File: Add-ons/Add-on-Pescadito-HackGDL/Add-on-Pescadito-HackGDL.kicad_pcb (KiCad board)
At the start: 2 copper layers, 153.2 x 94.5 mm, 96 parts, among them J1 Conn_02x03_Odd_Even, J2 Conn_02x03_Odd_Even, J3 Conn_02x03_Odd_Even, J4 Conn_02x03_Odd_Even, J5 Conn_02x03_Odd_Even, J6 Conn_02x03_Odd_Even, SW1 SW_RST, SW10 On, SW11 SW_RST, SW12 On, SW2 On, SW3 SW_RST, SW4 On, SW5 SW_RST, SW6 On, SW7 SW_RST, SW8 On, SW9 SW_RST, U1 PY32F002AA15M6TU, U2 PY32F002AA15M6TU, U3 PY32F002AA15M6TU, U4 PY32F002AA15M6TU, U5 PY32F002AA15M6TU, U6 PY32F002AA15M6TU

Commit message: feat(Hw):Update_Route_And_Init_Addon_Tortuguita
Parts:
- BT1, BT2, BT3, BT4, BT5, C1, C2, C3, C4, C5, J1, J2, J3, J4, J5, R1, R10, R11, R12, R13, R14, R15, R16, R17, R18, R19, R2, R20, R21, R22, R23, R24, R25, R3, R4, R5, R6, R7, R8, R9, SW1, SW10, SW2, SW3, SW4, SW5, SW6, SW7, SW8, SW9, U1, U2, U3, U4, U5: moved to B.Cu
- moved R15 295.1 mm to (222.6, 85.5), turned to 180 degrees
- moved R11 285.6 mm to (213.3, 67.9)
- moved R10 278.3 mm to (171.0, 85.5), turned to 180 degrees
- moved SW6 277.5 mm to (222.4, 64.7), turned to -41 degrees
- moved BT3 270.7 mm to (206.6, 84.9), turned to -15 degrees
- moved R6 269.4 mm to (161.7, 67.9)
- moved R13 264.2 mm to (191.4, 82.6), turned to -90 degrees
- moved SW5 264.2 mm to (208.5, 61.2), turned to 180 degrees
- moved D11 263.2 mm to (215.9, 66.1), turned to 139 degrees
- moved R12 262.7 mm to (190.6, 66.7)
- moved SW4 262.3 mm to (170.8, 64.7), turned to -41 degrees
- moved R14 253.8 mm to (181.7, 71.7), turned to -90 degrees
- moved J3 252.0 mm to (187.8, 85.2)
- moved BT2 250.9 mm to (155.0, 84.9), turned to -15 degrees
- moved D15 250.5 mm to (202.2, 85.1), turned to 155 degrees
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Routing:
- net /Pink_Fish/+3.3V: track 0.00 -> 77.2 mm, vias 0 -> 4
- net /Green_Fish/+3.3V: track 0.00 -> 76.1 mm, vias 0 -> 4
- net /Blue_Fish/+3.3V: track 0.00 -> 75.9 mm, vias 0 -> 4
- net /Red_Fish/+3.3V: track 0.00 -> 75.4 mm, vias 0 -> 4
- net /Orange_Fish/+3.3V: track 0.00 -> 74.6 mm, vias 0 -> 4
- net /Yellow_Fish/+3.3V: track 0.00 -> 74.2 mm, vias 0 -> 4
- net Net-(BT5--): track 0.00 -> 29.5 mm, vias 0 -> 2
- net Net-(BT4--): track 0.00 -> 29.3 mm, vias 0 -> 2
- net Net-(BT1--): track 0.00 -> 29.3 mm, vias 0 -> 2
- net Net-(BT3--): track 0.00 -> 29.1 mm, vias 0 -> 2
- net Net-(BT2--): track 0.00 -> 29.0 mm, vias 0 -> 2
- net Net-(BT6--): track 0.00 -> 28.8 mm, vias 0 -> 2
- net /Orange_Fish/PA6: track 0.00 -> 23.4 mm, vias 0 -> 1
- net /Pink_Fish/PA6: track 0.00 -> 23.4 mm, vias 0 -> 1
- net /Yellow_Fish/PA6: track 0.00 -> 23.4 mm, vias 0 -> 1
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- added copper zone on B.Cu, net /Blue_Fish/GND
- added copper zone on F.Cu, net /Blue_Fish/GND
- added copper zone on B.Cu, net /Green_Fish/GND
- added copper zone on F.Cu, net /Green_Fish/GND
- added copper zone on B.Cu, net /Orange_Fish/GND
- added copper zone on F.Cu, net /Orange_Fish/GND
- added copper zone on B.Cu, net /Pink_Fish/GND
- added copper zone on F.Cu, net /Pink_Fish/GND
- added copper zone on B.Cu, net /Red_Fish/GND
- added copper zone on F.Cu, net /Red_Fish/GND
- added copper zone on B.Cu, net /Yellow_Fish/GND
- added copper zone on F.Cu, net /Yellow_Fish/GND
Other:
- outline, holes or cut-outs redrawn

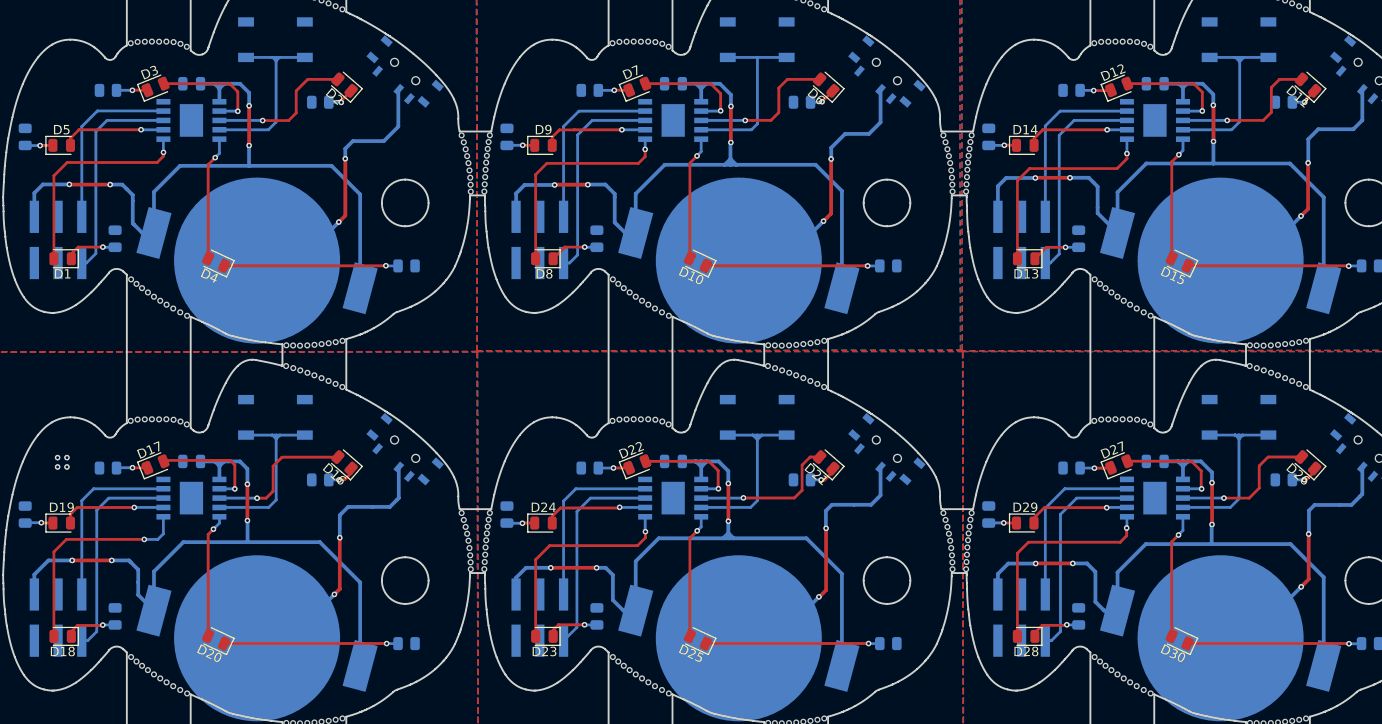
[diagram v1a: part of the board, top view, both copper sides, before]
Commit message: feat(Hw):Update_Labels
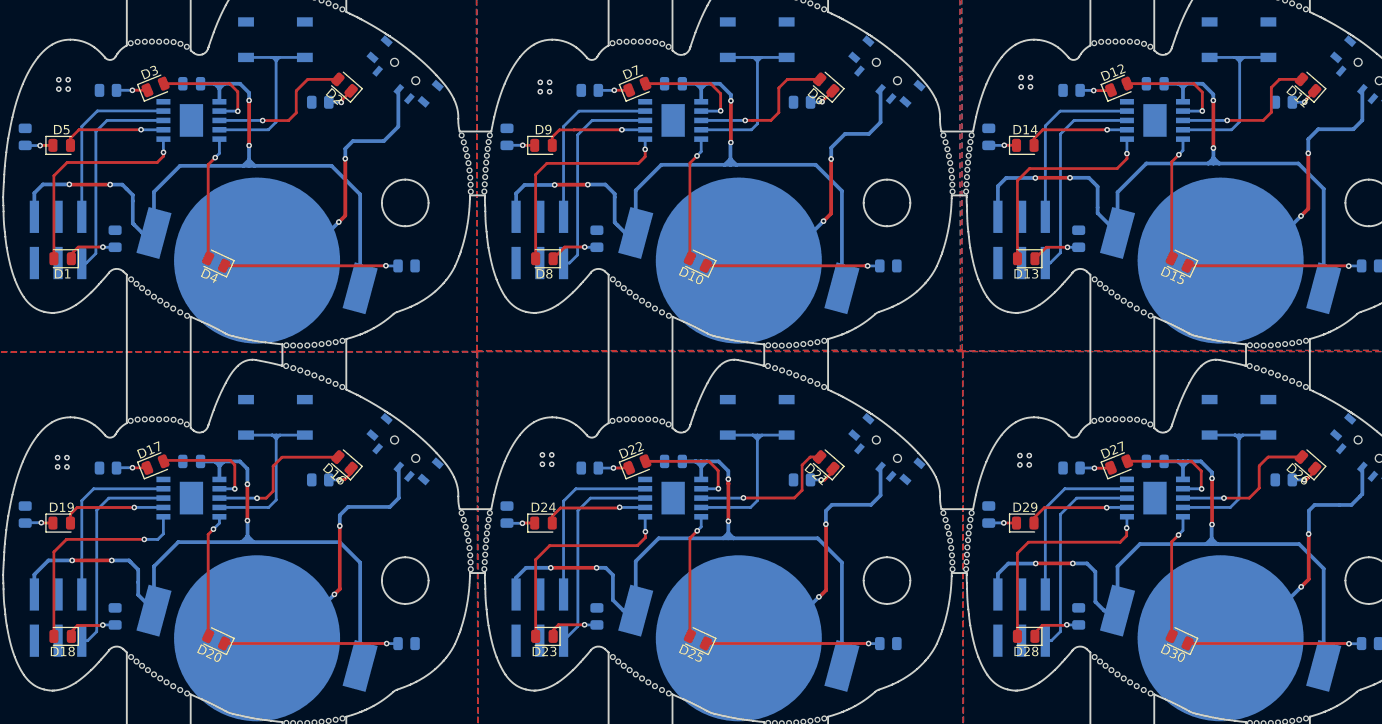
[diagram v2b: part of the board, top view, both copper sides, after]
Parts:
- added kibuzzard-684B03BD: G***, kibuzzard-684B03BD, B.Cu at (164.5, 64.3)
- added kibuzzard-684B03BD: G***, kibuzzard-684B03BD, B.Cu at (216.1, 104.7)
- added kibuzzard-684B03BD: G***, kibuzzard-684B03BD, B.Cu at (164.5, 104.7)
- added kibuzzard-684B03BD: G***, kibuzzard-684B03BD, B.Cu at (112.9, 64.3)
- added kibuzzard-684B03BD: G***, kibuzzard-684B03BD, B.Cu at (216.1, 64.3)
- added kibuzzard-684B03BD: G***, kibuzzard-684B03BD, B.Cu at (112.9, 104.7)
- added kibuzzard-684B03C9: G***, kibuzzard-684B03C9, B.Cu at (167.9, 108.6)
- added kibuzzard-684B03C9: G***, kibuzzard-684B03C9, B.Cu at (219.5, 108.6)
- added kibuzzard-684B03C9: G***, kibuzzard-684B03C9, B.Cu at (219.5, 68.2)
- added kibuzzard-684B03C9: G***, kibuzzard-684B03C9, B.Cu at (116.3, 68.2)
- added kibuzzard-684B03C9: G***, kibuzzard-684B03C9, B.Cu at (167.9, 68.2)
- added kibuzzard-684B03C9: G***, kibuzzard-684B03C9, B.Cu at (116.3, 108.6)
- added kibuzzard-68929515: G***, kibuzzard-68929515, B.Cu at (84.2, 77.5)
- added kibuzzard-68929515: G***, kibuzzard-68929515, B.Cu at (84.2, 117.9)
- added kibuzzard-68929515: G***, kibuzzard-68929515, B.Cu at (187.4, 77.5)
- added kibuzzard-68929515: G***, kibuzzard-68929515, B.Cu at (187.4, 117.9)
- added kibuzzard-68929515: G***, kibuzzard-68929515, B.Cu at (135.8, 77.5)
- added kibuzzard-68929515: G***, kibuzzard-68929515, B.Cu at (135.8, 117.9)
- added kibuzzard-68929520: G***, kibuzzard-68929520, B.Cu at (79.5, 117.9)
- added kibuzzard-68929520: G***, kibuzzard-68929520, B.Cu at (182.6, 77.5)
- added kibuzzard-68929520: G***, kibuzzard-68929520, B.Cu at (131.1, 117.9)
- added kibuzzard-68929520: G***, kibuzzard-68929520, B.Cu at (79.5, 77.5)
- added kibuzzard-68929520: G***, kibuzzard-68929520, B.Cu at (182.6, 117.9)
- added kibuzzard-68929520: G***, kibuzzard-68929520, B.Cu at (131.1, 77.5)
- added kibuzzard-6892952E: G***, kibuzzard-6892952E, B.Cu at (140.3, 125.3)
- added kibuzzard-6892952E: G***, kibuzzard-6892952E, B.Cu at (140.3, 84.8)
- added kibuzzard-6892952E: G***, kibuzzard-6892952E, B.Cu at (88.7, 125.3)
- added kibuzzard-6892952E: G***, kibuzzard-6892952E, B.Cu at (191.9, 84.8)
- added kibuzzard-6892952E: G***, kibuzzard-6892952E, B.Cu at (191.9, 125.3)
- added kibuzzard-6892952E: G***, kibuzzard-6892952E, B.Cu at (88.8, 84.8)
- added kibuzzard-697CCF2B: G***, kibuzzard-697CCF2B, B.Cu at (79.9, 87.9)
- added kibuzzard-697CCF2B: G***, kibuzzard-697CCF2B, B.Cu at (131.5, 87.9)
- added kibuzzard-697CCF2B: G***, kibuzzard-697CCF2B, B.Cu at (183.1, 87.9)
- added kibuzzard-697CCF2B: G***, kibuzzard-697CCF2B, B.Cu at (183.1, 128.4)
- added kibuzzard-697CCF2B: G***, kibuzzard-697CCF2B, B.Cu at (79.9, 128.4)
- added kibuzzard-697CCF2B: G***, kibuzzard-697CCF2B, B.Cu at (131.5, 128.4)
- D10, D7, D8, D9: value Red -> Pink
- D11, D16, D2, D21, D26, D6: value Red -> White
- D12, D13, D14, D15: value Red -> Blue
- D17, D18, D19, D20: value Red -> Yellow
- D22, D23, D24, D25: value Red -> Green
- D27, D28, D29, D30: value Red -> Orange
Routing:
- net /Yellow_Fish/+3.3V: track 74.2 -> 77.6 mm
- net /Orange_Fish/+3.3V: track 74.6 -> 77.1 mm
- net /Blue_Fish/+3.3V: track 75.9 -> 78.1 mm
- net /Red_Fish/+3.3V: track 75.4 -> 77.2 mm
- net /Pink_Fish/NRST: track 19.7 -> 21.0 mm
- net /Green_Fish/+3.3V: track 76.1 -> 76.8 mm
- net /Red_Fish/GND: vias 0 -> 4
- net /Pink_Fish/GND: vias 0 -> 4
- net /Orange_Fish/GND: vias 0 -> 4
- net /Green_Fish/GND: vias 0 -> 4
- net /Blue_Fish/GND: vias 0 -> 4
